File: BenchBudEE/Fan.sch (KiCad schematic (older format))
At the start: 11 parts, among them Q2 DMN65D8L-7, Q3 AOD476, Q4 AOD476, U10 MCP4801, U4 OPA4170

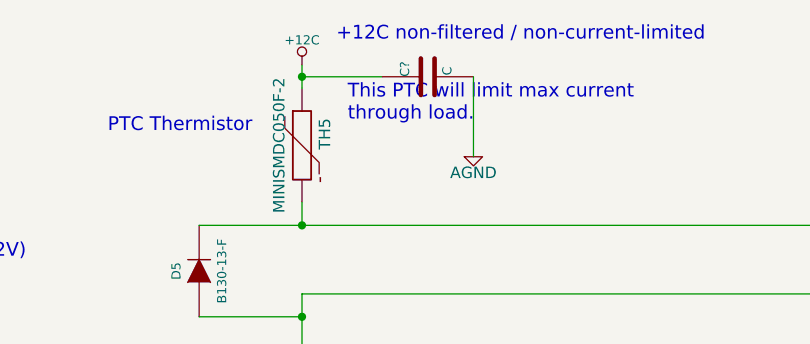
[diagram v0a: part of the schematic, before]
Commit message: Roughly placed the current/fan driver module components.
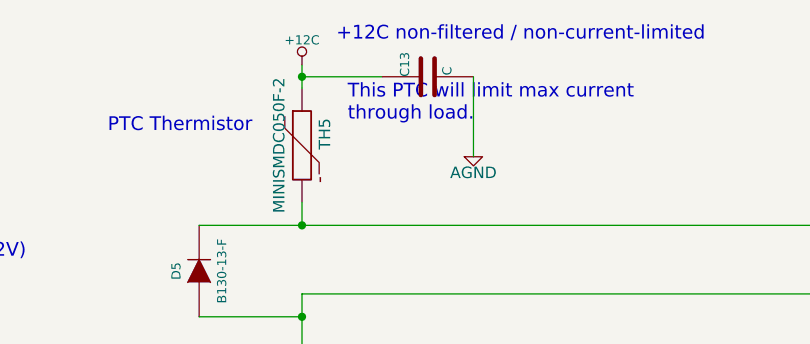
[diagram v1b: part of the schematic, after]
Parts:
- removed Q3, Q4: AOD476, ~, symbol MOSFET_N
- added Q3, Q4: AOD476, ~, symbol MOS_N_NUM
- gave numbers to parts that had none: 1
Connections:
- net +5V: now also Q3.3 (S)
- net CURR_MEAS: now also Q3.2 (D), Q4.3 (S)
- net FAN_MODE: now also Q3.1 (G)
- net FAN_OUT-: now also Q4.2 (D)
- net at U4.7: now also Q4.1 (G)
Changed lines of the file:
@@
-	1    0    0    -1
-$EndComp
-$Comp
-L MOSFET_N Q4
-U 1 1 52F362B9
-P 7700 2700
-F 0 "Q4" H 7710 2870 60  0000 R CNN
-F 1 "AOD476" H 7710 2550 60  0000 R CNN
-F 2 "~" H 7700 2700 60  0000 C CNN
-F 3 "~" H 7700 2700 60  0000 C CNN
-F 4 "Alpha & Omega" H 7700 2700 60  0001 C CNN "MFG Name"
-F 5 "AOD476" H 7700 2700 60  0001 C CNN "MFG Part Number"
-	1    7700 2700
 	1    0    0    -1
 $EndComp
@@
 $EndComp
 $Comp
-L AGND #PWR58
+L AGND #PWR048
 U 1 1 52F3630D
 P 7800 5300
-F 0 "#PWR58" H 7800 5300 40  0001 C CNN
+F 0 "#PWR048" H 7800 5300 40  0001 C CNN
 F 1 "AGND" H 7800 5230 50  0000 C CNN
 F 2 "" H 7800 5300 60  0000 C CNN
@@
 Connection ~ 7800 4050
 $Comp
-L +12V #PWR55
+L +12V #PWR049
 U 1 1 52F36343
 P 6250 1750
-F 0 "#PWR55" H 6250 1700 20  0001 C CNN
+F 0 "#PWR049" H 6250 1700 20  0001 C CNN
 F 1 "+12V" H 6250 1850 30  0000 C CNN
 F 2 "" H 6250 1750 60  0000 C CNN
@@
 	6250 1750 6250 2300
 $Comp
-L -12V #PWR56
+L -12V #PWR050
 U 1 1 52F36356
 P 6250 3350
-F 0 "#PWR56" H 6250 3480 20  0001 C CNN
+F 0 "#PWR050" H 6250 3480 20  0001 C CNN
 F 1 "-12V" H 6250 3450 30  0000 C CNN
 F 2 "" H 6250 3350 60  0000 C CNN
@@
 	4400 2600 5850 2600
 $Comp
-L AGND #PWR54
+L AGND #PWR051
 U 1 1 52F36460
 P 5150 3700
-F 0 "#PWR54" H 5150 3700 40  0001 C CNN
+F 0 "#PWR051" H 5150 3700 40  0001 C CNN
 F 1 "AGND" H 5150 3630 50  0000 C CNN
 F 2 "" H 5150 3700 60  0000 C CNN
@@
 Text Notes 2850 1950 0    60   ~ 0
 DAC
-$Comp
-L MOSFET_N Q3
-U 1 1 52FADC41
-P 7200 4650
-F 0 "Q3" H 7210 4820 60  0000 R CNN
-F 1 "AOD476" H 7210 4500 60  0000 R CNN
-F 2 "~" H 7200 4650 60  0000 C CNN
-F 3 "~" H 7200 4650 60  0000 C CNN
-F 4 "Alpha & Omega" H 7200 4650 60  0001 C CNN "MFG Name"
-F 5 "AOD476" H 7200 4650 60  0001 C CNN "MFG Part Number"
-	1    7200 4650
-	1    0    0    -1
-$EndComp
 $Comp
 L THERMISTOR TH5
@@
 Filtered Rail (12V)
 $Comp
-L +12C #PWR57
+L +12C #PWR052
 U 1 1 52FAE969
 P 7800 750
-F 0 "#PWR57" H 7800 720 30  0001 C CNN
+F 0 "#PWR052" H 7800 720 30  0001 C CNN
 F 1 "+12C" H 7800 860 40  0000 C CNN
 F 2 "" H 7800 750 60  0000 C CNN
@@
 Connection ~ 2650 1450
 $Comp
-L AGND #PWR51
+L AGND #PWR053
 U 1 1 53090CFD
 P 2000 1600
-F 0 "#PWR51" H 2000 1600 40  0001 C CNN
+F 0 "#PWR053" H 2000 1600 40  0001 C CNN
 F 1 "AGND" H 2000 1530 50  0000 C CNN
 F 2 "" H 2000 1600 60  0000 C CNN
@@
 Connection ~ 2100 1450
 $Comp
-L +5V #PWR52
+L +5V #PWR054
 U 1 1 53090D05
 P 2650 1300
-F 0 "#PWR52" H 2650 1390 20  0001 C CNN
+F 0 "#PWR054" H 2650 1390 20  0001 C CNN
 F 1 "+5V" H 2650 1390 30  0000 C CNN
 F 2 "" H 2650 1300 60  0000 C CNN
@@
 $EndComp
 $Comp
-L AGND #PWR53
+L AGND #PWR055
 U 1 1 53090D0B
 P 2650 3650
-F 0 "#PWR53" H 2650 3650 40  0001 C CNN
+F 0 "#PWR055" H 2650 3650 40  0001 C CNN
 F 1 "AGND" H 2650 3580 50  0000 C CNN
 F 2 "" H 2650 3650 60  0000 C CNN
@@
 PTC Thermistor
 $Comp
-L C C?
+L C C13
 U 1 1 5308A319
 P 8350 800
-F 0 "C?" H 8350 900 40  0000 L CNN
+F 0 "C13" H 8350 900 40  0000 L CNN
 F 1 "C" H 8356 715 40  0000 L CNN
 F 2 "~" H 8388 650 30  0000 C CNN
@@
 Connection ~ 7800 800
 $Comp
-L AGND #PWR?
+L AGND #PWR056
 U 1 1 5308A34F
 P 8550 1150
-F 0 "#PWR?" H 8550 1150 40  0001 C CNN
+F 0 "#PWR056" H 8550 1150 40  0001 C CNN
 F 1 "AGND" H 8550 1080 50  0000 C CNN
 F 2 "" H 8550 1150 60  0000 C CNN
@@
 Wire Wire Line
 	8550 1150 8550 800
+$Comp
+L MOS_N_NUM Q4
+U 1 1 53092CDC
+P 7700 2700
+F 0 "Q4" H 7710 2870 60  0000 R CNN
+F 1 "AOD476" H 7710 2550 60  0000 R CNN
+F 2 "~" H 7700 2700 60  0000 C CNN
+F 3 "~" H 7700 2700 60  0000 C CNN
+F 4 "Alpha & Omega" H 7700 2700 60  0001 C CNN "MFG Name"
+F 5 "AOD476" H 7700 2700 60  0001 C CNN "MFG Part Number"
+	1    7700 2700
+	1    0    0    -1
+$EndComp
+$Comp
+L MOS_N_NUM Q3
+U 1 1 53092D7D
+P 7200 4650
+F 0 "Q3" H 7210 4820 60  0000 R CNN
+F 1 "AOD476" H 7210 4500 60  0000 R CNN
+F 2 "~" H 7200 4650 60  0000 C CNN
+F 3 "~" H 7200 4650 60  0000 C CNN
+F 4 "Alpha & Omega" H 7200 4650 60  0001 C CNN "MFG Name"
+F 5 "AOD476" H 7200 4650 60  0001 C CNN "MFG Part Number"
+	1    7200 4650
+	1    0    0    -1
+$EndComp
 $EndSCHEMATC
